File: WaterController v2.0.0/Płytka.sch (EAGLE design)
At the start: 77 parts, among them IC1 DS1307ZN+, IC2 LM2576S/5V, J1 HUM1, J2 HUM2, J3 TEMP, J4 SUN, Q1 AOD2922, Q2 AOD2922, Q4 BSS138, Q5 BSS138, U1 ESP-WROOM-32, U2 LM3940IMP-3.3

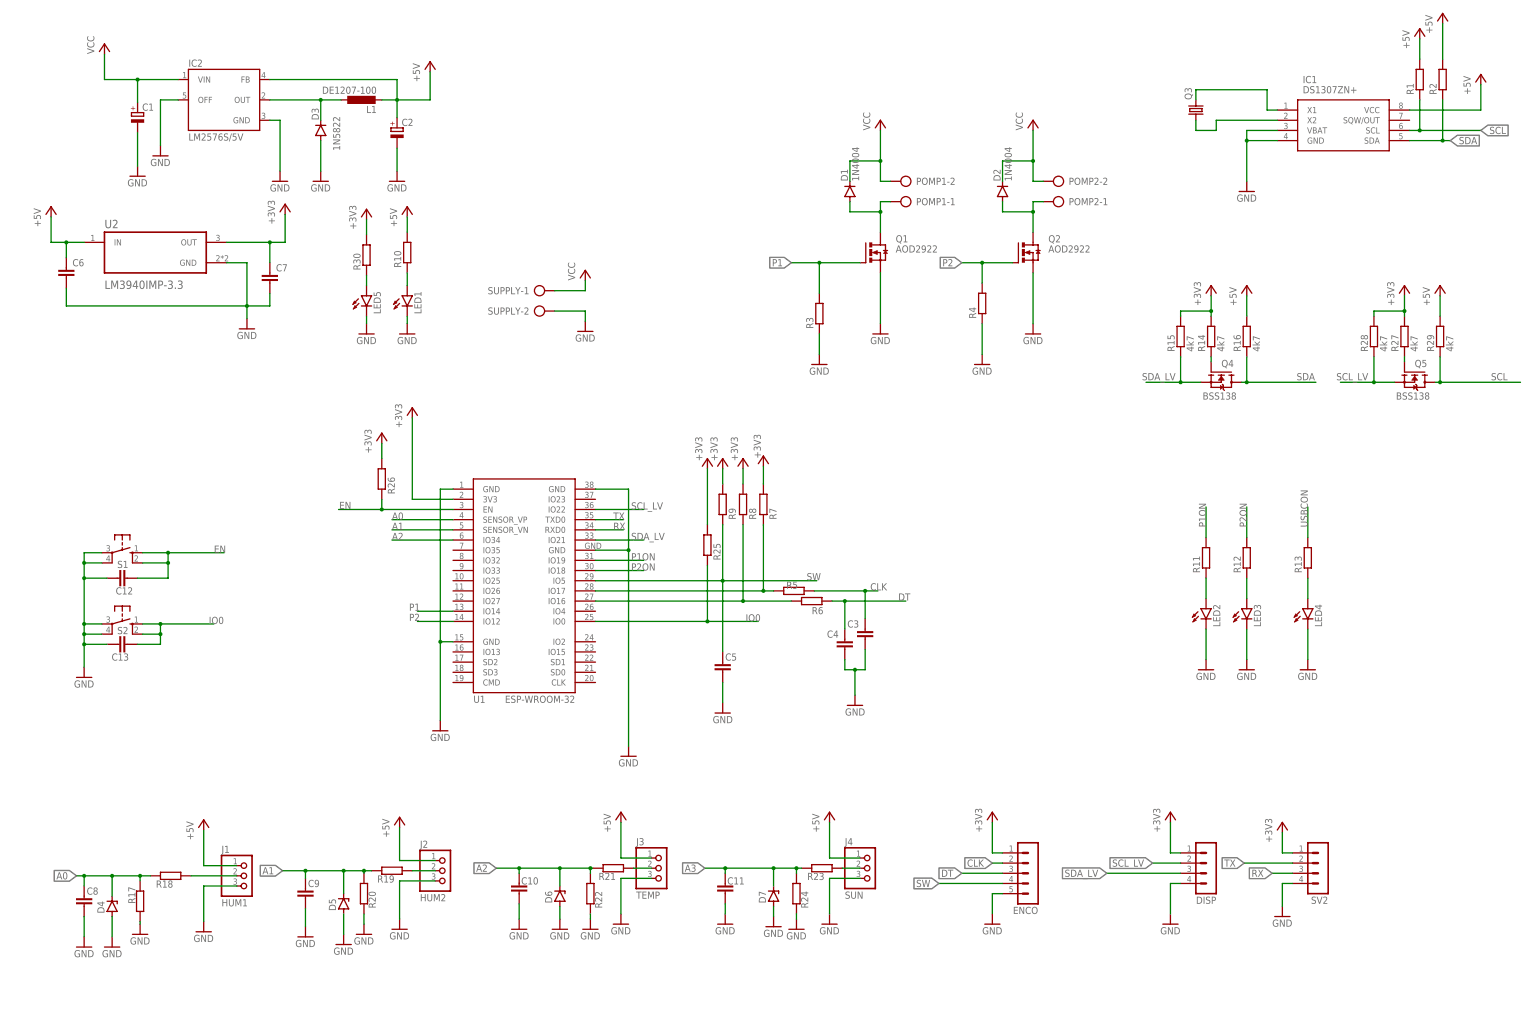
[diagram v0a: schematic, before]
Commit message: Add new board from another project
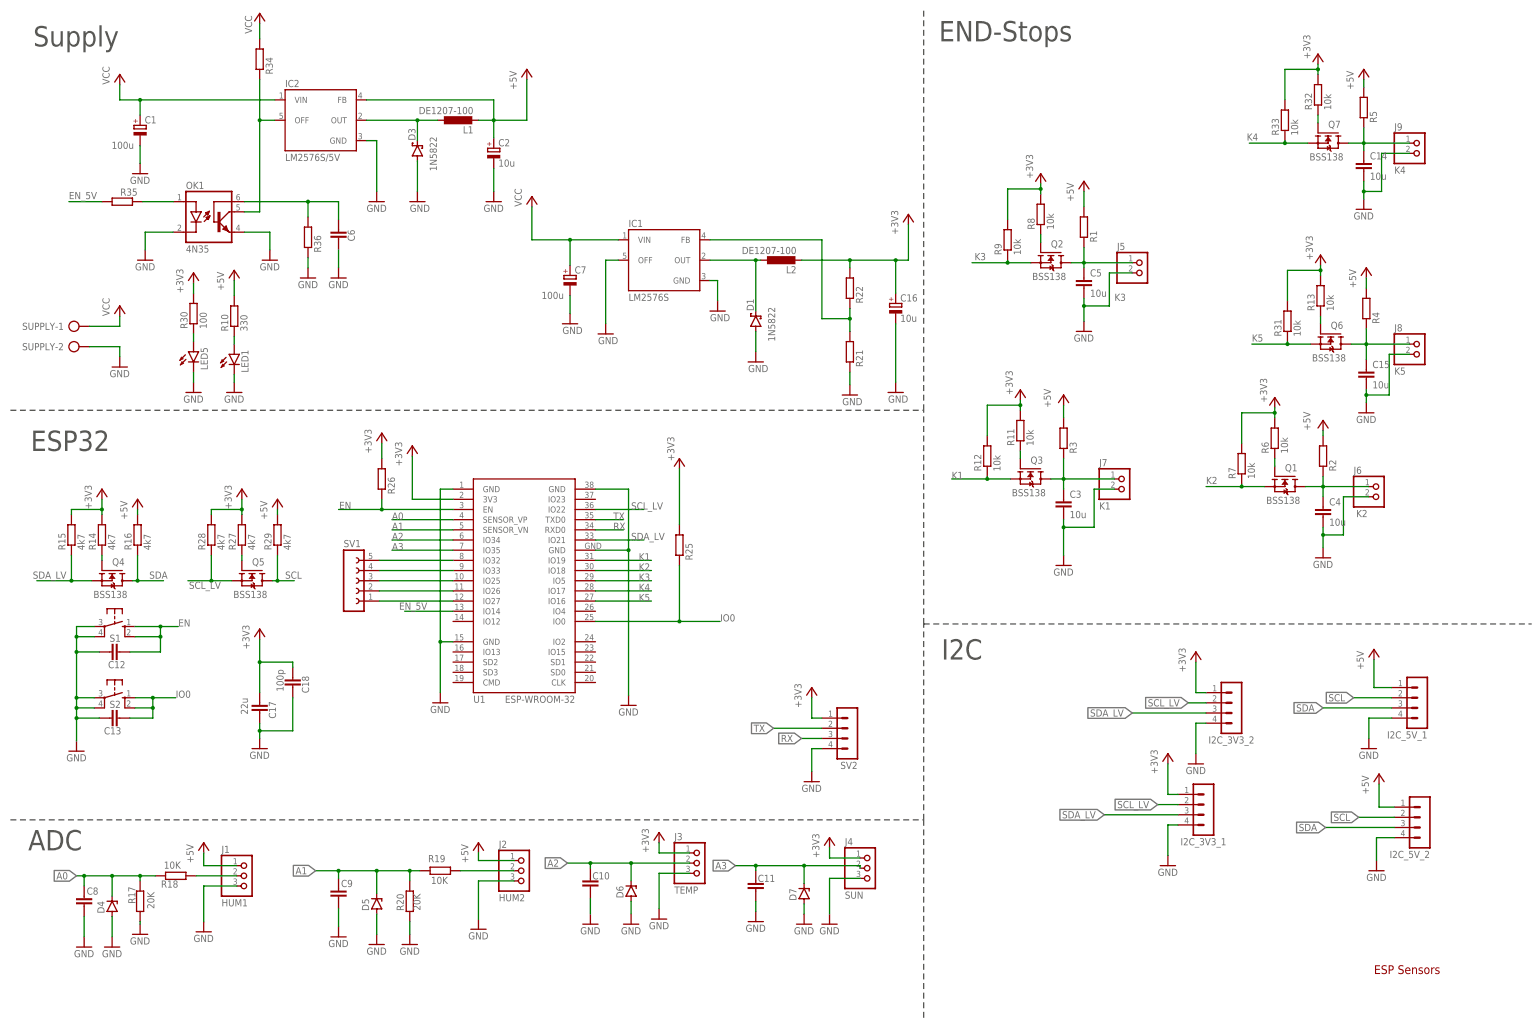
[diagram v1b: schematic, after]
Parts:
- removed D2: 1N4004, diode:1N4004
- removed DISP: (no value), con-lstb:MA04-1
- removed ENCO: (no value), con-lstb:MA05-1
- removed LED2, LED3, LED4: (no value), led:LEDSML0805
- removed POMP1, POMP2: (no value), con-ptr500:AK500/2-H
- removed R23, R24: (no value), rcl:R-EU_R0805
- removed U2: LM3940IMP-3.3, LM3940IMP-3.3:LM3940IMP-3.3
- added C14, C15: 10u, rcl:C-EUC0805K
- added C16: 10u, rcl:CPOL-EUE3.5-8
- added C17: 22u, rcl:C-EUC0805K
- added C18: 100p, rcl:C-EUC0805K
- added I2C_3V3_1, I2C_3V3_2, I2C_5V_1, I2C_5V_2: (no value), con-lstb:MA04-1
- added J5: K3, PUTRocketLab_connectors:WT-2MM-2PINSTRAIGHT
- added J6: K2, PUTRocketLab_connectors:WT-2MM-2PINSTRAIGHT
- added J7: K1, PUTRocketLab_connectors:WT-2MM-2PINSTRAIGHT
- added J8: K5, PUTRocketLab_connectors:WT-2MM-2PINSTRAIGHT
- added J9: K4, PUTRocketLab_connectors:WT-2MM-2PINSTRAIGHT
- added L2: DE1207-100, ferrocore:DE1207-100
- added OK1: 4N35, optocoupler:4N35
- added Q6, Q7: BSS138, bss138_10:BSS138
- added R31, R32, R33: 10k, rcl:R-EU_R0805
- added R34, R35, R36: (no value), rcl:R-EU_R0805
- added SV1: (no value), con-lsta:FE05-1
- C1: value (none) -> 100u
- C2: value (none) -> 10u; device rcl:CPOL-EUE2.5-6 -> rcl:CPOL-EUE3.5-8
- C3, C4, C5: value (none) -> 10u
- C7: value (none) -> 100u; device rcl:C-EUC0805K -> rcl:CPOL-EUE2.5-6
- D1: value 1N4004 -> 1N5822; device diode:1N4004 -> diode:1N5908
- D3: device diode:1N4004 -> diode:1N5908
- IC1: value DS1307ZN+ -> LM2576S; device DS1307ZN+:DS1307ZN+ -> v-reg-3:LM2576S
- IC2: device v-reg-3:LM2576S -> v-reg-3:LM2576T
- Q1, Q2: value AOD2922 -> BSS138; device transistor-power:IRF3704S -> bss138_10:BSS138
- Q3: value (none) -> BSS138; device crystal:CRYSTALTC26H -> bss138_10:BSS138
- R10: value (none) -> 330
- R11, R12, R13, R6, R7, R8, R9: value (none) -> 10k
- R17, R20: value (none) -> 20K
- R18, R19: value (none) -> 10K
- R30: value (none) -> 100
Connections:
- removed net CLK: C3.1, ENCO.2, R5.2
- removed net DT: C4.1, ENCO.3, R6.2
- removed net N$15: J4.2, R23.1
- removed net P1: Q1.G, R3.2, U1.IO14
- removed net P1ON: R11.2, U1.IO19
- removed net P2: Q2.G, R4.2, U1.IO12
- removed net P2ON: R12.2, U1.IO18
- removed net SW: C5.1, ENCO.4, R9.1, U1.IO5
- removed net USBCON: R13.2
- new net EN_5V: R35.2, U1.IO14
- new net K1: Q3.S, R12.1, U1.IO19
- new net K2: Q1.S, R7.1, U1.IO18
- new net K3: Q2.S, R9.1, U1.IO5
- new net K4: Q7.S, R33.1, U1.IO17
- new net K5: Q6.S, R31.1, U1.IO16
- new net N$14: SV1.3, U1.IO25
- new net N$16: Q3.G, R11.1
- new net N$17: SV1.2, U1.IO26
- new net N$20: Q6.G, R13.1
- new net N$22: SV1.1, U1.IO27
- new net N$24: Q7.G, R32.1
- new net N$25: IC2.OFF, OK1.COL, R34.1
- new net N$26: OK1.A, R35.1
- new net N$29: C6.2, OK1.BAS, R36.2
- new net N$30: IC1.FB, R21.2, R22.1
- net +3V3: now also C16.+, C17.2, C18.2, I2C_3V3_1.1, I2C_3V3_2.1, J3.1, J4.1, L2.2, R11.2, R12.2, R13.2, R22.2, R31.2, R32.2, R33.2, R6.2; no longer C7.1, U2.OUT
- net +5V: now also I2C_5V_1.1, I2C_5V_2.1, R3.2, R4.2, R5.2; no longer C6.1, DISP.1, ENCO.1, IC1.VCC, J3.1, J4.1, U2.IN
- net A2: now also J3.2; no longer R21.2, R22.1
- net A3: now also J4.2, U1.IO35; no longer R23.2, R24.1
- net GND: now also C14.2, C15.2, C16.-, C17.1, C18.1, C6.1, C7.-, D1.A, I2C_3V3_1.4, I2C_3V3_2.4, I2C_5V_1.4, I2C_5V_2.4, IC1.OFF, J5.2, J6.2, J7.2, J8.2, J9.2, OK1.C, OK1.EMI, R21.1, R36.1; no longer C6.2, C7.2, DISP.4, ENCO.5, IC1.VBAT, IC2.OFF, LED2.C, LED3.C, LED4.C, Q1.S, Q2.S, R22.2, R24.2, R3.1, R4.1, U2.GND
- net N$1: now also C5.1, J5.1, Q2.D, R1.1; no longer R5.1, R7.1, U1.IO17
- net N$10: now also SV1.5, U1.IO32; no longer IC1.X1, Q3.2
- net N$11: now also Q1.G, R6.1; no longer IC1.X2, Q3.1
- net N$12: now also SV1.4, U1.IO33; no longer D1.A, POMP1-1.KL, Q1.D
- net N$13: now also Q2.G, R8.1; no longer D2.A, POMP2-1.KL, Q2.D
- net N$2: now also C4.1, J6.1, Q1.D, R2.1; no longer R6.1, R8.1, U1.IO16
- net N$21: now also D1.C, IC1.OUT, L2.1; no longer J3.2, R21.1
- net N$5: now also C3.1, J7.1, Q3.D, R3.1; no longer LED2.A, R11.1
- net N$6: now also C14.1, J9.1, Q7.D, R5.1; no longer LED3.A, R12.1
- net N$7: now also C15.1, J8.1, Q6.D, R4.1; no longer LED4.A, R13.1
- net SCL: now also I2C_5V_1.2, I2C_5V_2.2; no longer IC1.SCL, R1.1
- net SCL_LV: now also I2C_3V3_1.2, I2C_3V3_2.2; no longer DISP.2
- net SDA: now also I2C_5V_1.3, I2C_5V_2.3; no longer IC1.SDA, R2.1
- net SDA_LV: now also I2C_3V3_1.3, I2C_3V3_2.3; no longer DISP.3
- net VCC: now also C7.+, IC1.VIN, R34.2; no longer D1.C, D2.C, POMP1-2.KL, POMP2-2.KL
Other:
- note added: "ADC"
- note added: "END-Stops"
- note added: "ESP Sensors"
- note added: "ESP32"
- note added: "I2C"
- note added: "Supply"
- moved on the sheet: C1, C10, C11, C12, C13, C2, C3, C4, C5, C6, C9, D5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

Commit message: Create new board
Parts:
- removed C14, C15: 10u, rcl:C-EUC0805K
- removed J8: K5, PUTRocketLab_connectors:WT-2MM-2PINSTRAIGHT
- removed J9: K4, PUTRocketLab_connectors:WT-2MM-2PINSTRAIGHT
- removed R13, R31, R32, R33: 10k, rcl:R-EU_R0805
- added D2, D8: (no value), diode:DIODE-DO214AC
- added X1: + P2, con-ptr500:AK500/4
- Q6, Q7: value BSS138 -> AOD2922; device bss138_10:BSS138 -> Clean-Kong:MOSFET_NIXTY8N65X2
- R4, R5: value (none) -> 10K
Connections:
- removed net K4: Q7.S, R33.1, U1.IO17
- removed net K5: Q6.S, R31.1, U1.IO16
- removed net N$20: Q6.G, R13.1
- removed net N$24: Q7.G, R32.1
- new net P1: Q6.G, R4.2, U1.IO19
- new net P2: Q7.G, R5.2, U1.IO18
- net +3V3: no longer R13.2, R31.2, R32.2, R33.2
- net +5V: no longer R4.2, R5.2
- net GND: now also Q6.S, Q7.S, R4.1, R5.1; no longer C14.2, C15.2, J8.2, J9.2
- net K1: now also U1.IO5; no longer U1.IO19
- net K2: now also U1.IO17; no longer U1.IO18
- net K3: now also U1.IO16; no longer U1.IO5
- net N$6: now also D2.A, Q6.D, X1-2.KL; no longer C14.1, J9.1, Q7.D, R5.1
- net N$7: now also D8.A, Q7.D, X1-4.KL; no longer C15.1, J8.1, Q6.D, R4.1
- net VCC: now also D2.C, D8.C, X1-1.KL, X1-3.KL
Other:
- moved on the sheet: C3, C4, C5, J5, J6, J7, Q1, Q2, Q3, R1, R11, R12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

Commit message: improve board schematic
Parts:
- R22: value (none) -> 1k69
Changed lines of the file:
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@@
 <?xml version="1.0" encoding="utf-8"?>
 <!DOCTYPE eagle SYSTEM "eagle.dtd">
-<eagle version="9.5.1">
+<eagle version="9.6.2">
 <drawing>
 <settings>
@@
 <part name="IC1" library="v-reg-3" deviceset="LM2576" device="S"/>
 <part name="R21" library="rcl" library_urn="urn:adsk.eagle:library:334" deviceset="R-EU_" device="R0805" package3d_urn="urn:adsk.eagle:package:23553/2"/>
-<part name="R22" library="rcl" library_urn="urn:adsk.eagle:library:334" deviceset="R-EU_" device="R0805" package3d_urn="urn:adsk.eagle:package:23553/2"/>
+<part name="R22" library="rcl" library_urn="urn:adsk.eagle:library:334" deviceset="R-EU_" device="R0805" package3d_urn="urn:adsk.eagle:package:23553/2" value="1k69"/>
 <part name="GND25" library="supply1" library_urn="urn:adsk.eagle:library:371" deviceset="GND" device=""/>
 <part name="GND26" library="supply1" library_urn="urn:adsk.eagle:library:371" deviceset="GND" device=""/>
